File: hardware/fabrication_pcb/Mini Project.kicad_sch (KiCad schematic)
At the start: 14 parts, among them U1 DM-OLED096-636

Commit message: update footprints and symbols
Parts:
- ESP32, MIC1, Speaker1, amp1, nrf1: value ~ -> (none)

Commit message: feat: updated pcb layout
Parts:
- removed Speaker1: (no value), MyFootprints:0.25W_8OHM_SPEAKER, symbol MyComponents:SPEAKER
- added J1: Speaker, Connector_PinHeader_2.54mm:PinHeader_1x02_P2.54mm_Vertical, symbol Connector:Conn_01x02_Socket
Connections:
- net GND: now also C1.1, nrf1.1 (GND), J1.2 (Pin_2); no longer C1.2, nrf1.2 (VCC)
- net VCC: now also C1.2, nrf1.2 (VCC); no longer C1.1, nrf1.1 (GND)
- net at amp1.5 (OUT): now also J1.1 (Pin_1)
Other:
- title: (none) -> FELCOM-HW

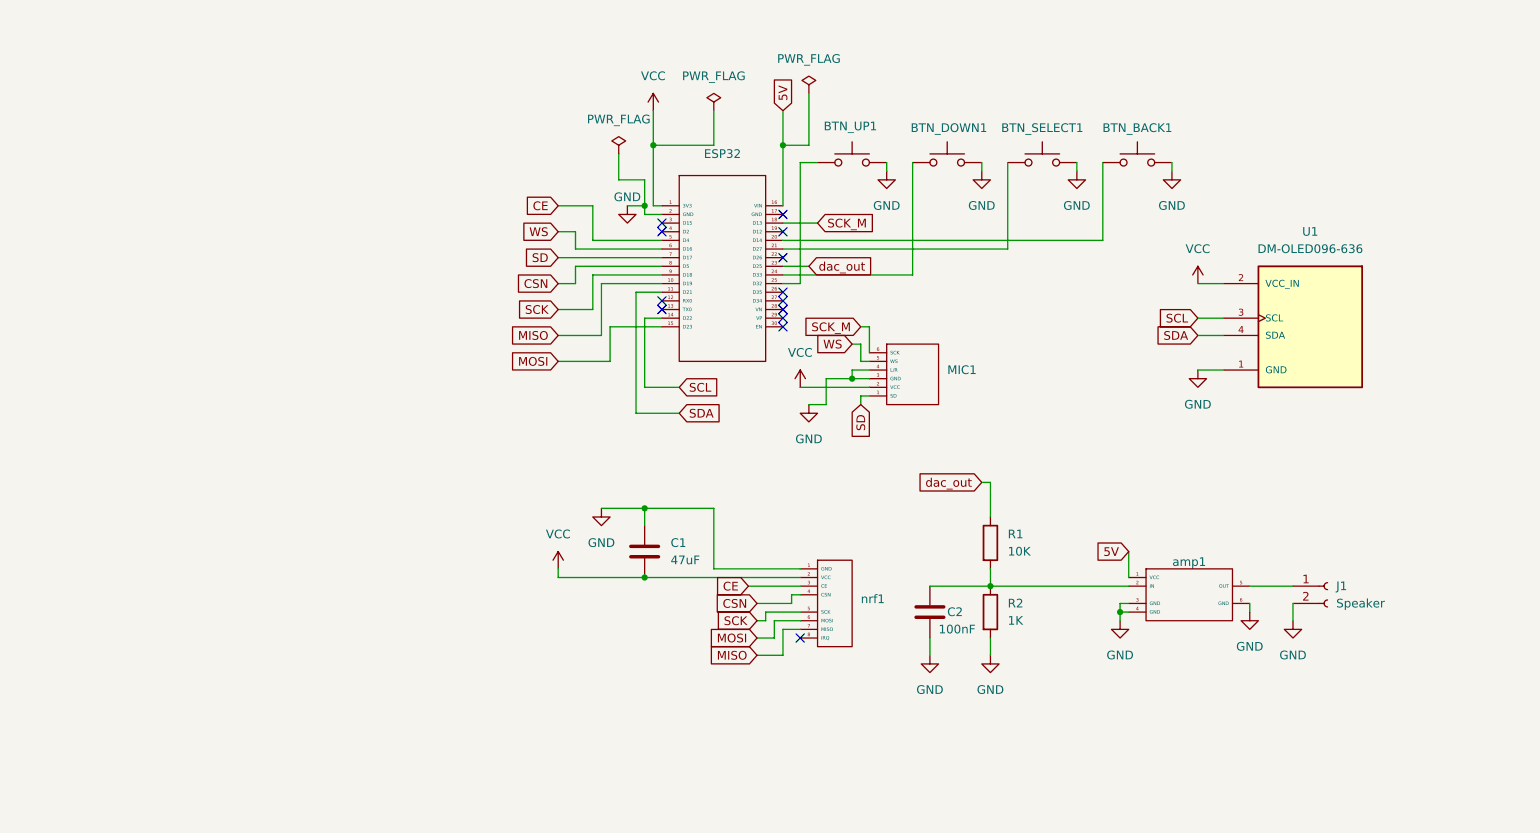
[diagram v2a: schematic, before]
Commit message: fix: schematic looking fancy, component placement done
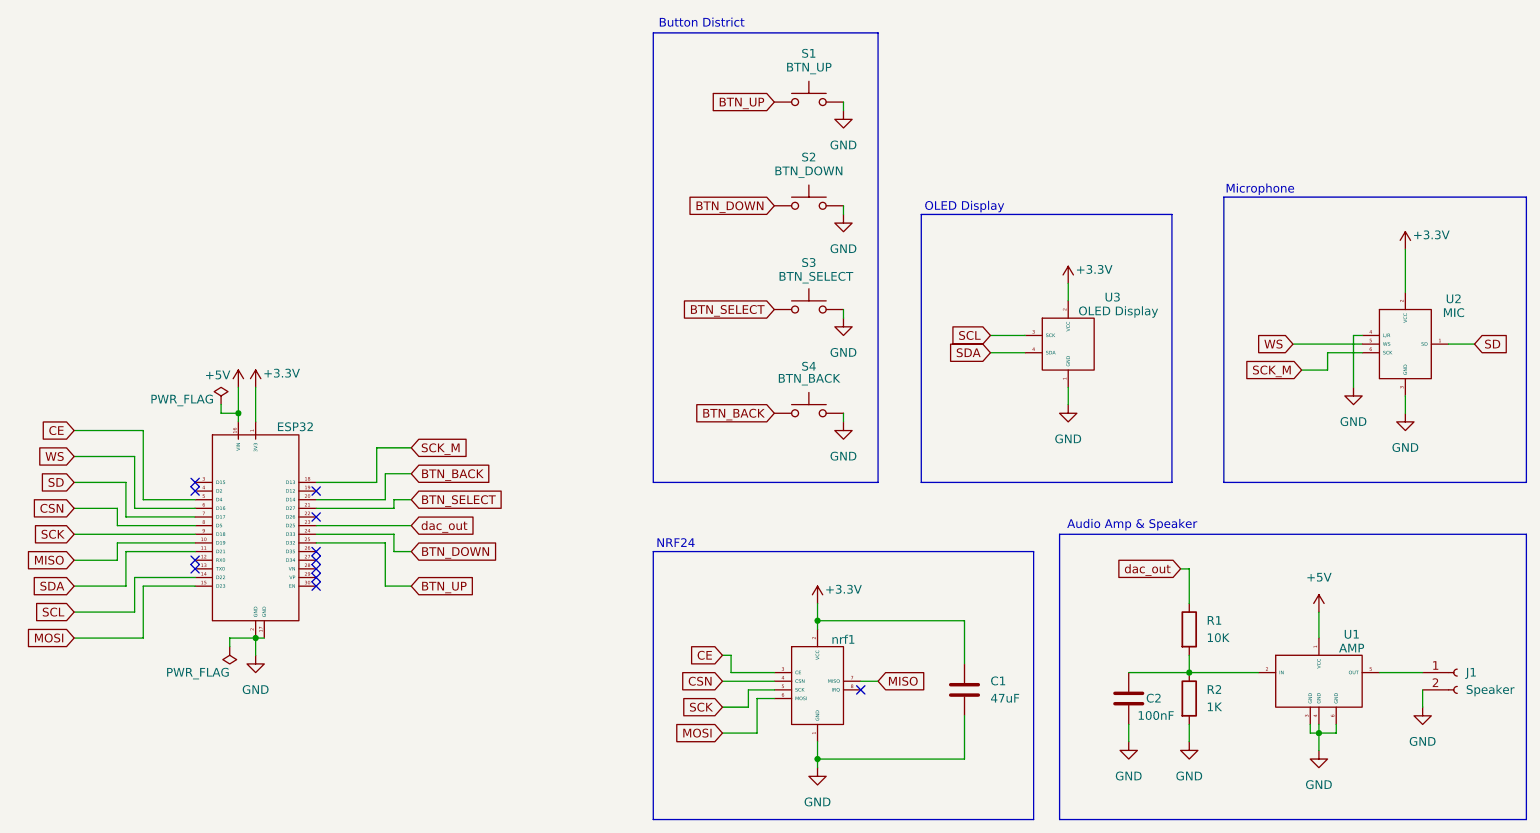
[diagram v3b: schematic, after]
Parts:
- removed MIC1: (no value), MyFootprints:MH-ET_I2S_MICROPHONE_MODULE, symbol MyComponents:MH-ET_I2S_MICROPHONE_MODULE
- removed U1: DM-OLED096-636, MyFootprints:MODULE_DM-OLED096-636, symbol DM-OLED096-636:DM-OLED096-636
- added U2: MIC, MyFootprints:MH-ET_I2S_MICROPHONE_MODULE, symbol MyComponents:MH-ET_I2S_MICROPHONE_MODULE
- added U3: OLED Display, MyFootprints:MODULE_DM-OLED096-636, symbol MyComponents:OLED_128x64_I2C
- S1: renamed from BTN_UP1; value SW_Push -> BTN_UP
- S2: renamed from BTN_DOWN1; value SW_Push -> BTN_DOWN
- S3: renamed from BTN_SELECT1; value SW_Push -> BTN_SELECT
- S4: renamed from BTN_BACK1; value SW_Push -> BTN_BACK
- U1: renamed from amp1; value (none) -> AMP
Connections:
- net GND: now also C1.2, ESP32.17 (GND), S2.1, U2.3 (GND), U2.4 (L/R), U3.1 (GND); no longer C1.1, S2.2
- net SCK_M: now also U2.6 (SCK)
- net SCL: now also U3.3 (SCK)
- net SD: now also U2.1 (SD)
- net SDA: now also U3.4 (SDA)
- net WS: now also U2.5 (WS)
- net BTN_DOWN: now reaches ESP32.24 (D33)
- net BTN_DOWN: now also S2.2; no longer S2.1
- net BTN_BACK: now reaches ESP32.20 (D14), S4.1
- net BTN_UP: now reaches ESP32.25 (D32), S1.1
- net BTN_SELECT: now reaches ESP32.21 (D27), S3.1
- net 5V renamed +5V
- net VCC renamed +3.3V
- net +3.3V: now also C1.1, U2.2 (VCC), U3.2 (VCC); no longer C1.2
- no-connect marks 13 -> 12
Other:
- note added: "Audio Amp & Speaker"
- note added: "Button District"
- note added: "Microphone"
- note added: "NRF24"
- note added: "OLED Display"
- moved on the sheet: C1, C2, ESP32, J1, R1, R2, S1, S2, S3, S4, U1, nrf1

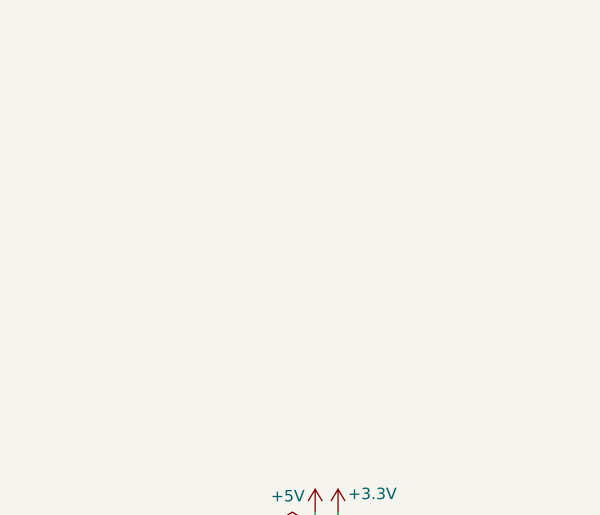
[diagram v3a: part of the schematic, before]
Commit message: feat: mount holes
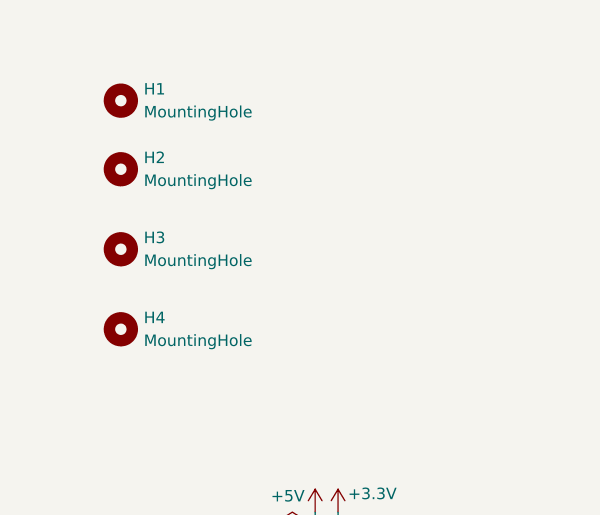
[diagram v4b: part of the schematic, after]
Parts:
- added H1, H2, H3, H4: MountingHole, MountingHole:MountingHole_3.2mm_M3, symbol Mechanical:MountingHole

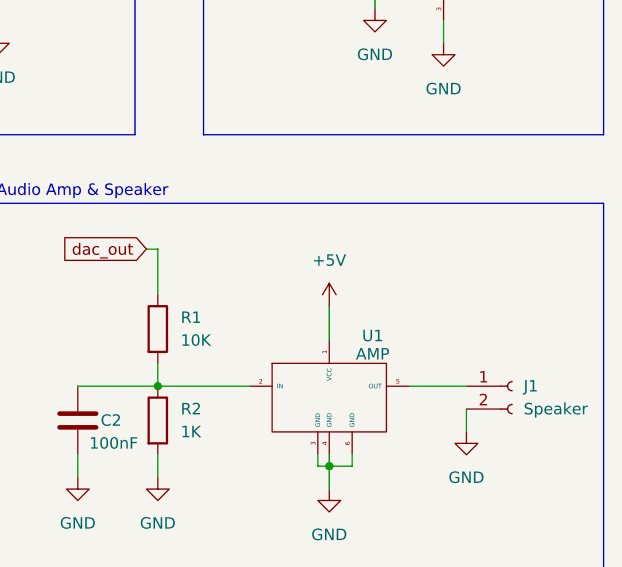
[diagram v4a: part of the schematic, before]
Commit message: Feat: silkscreen art
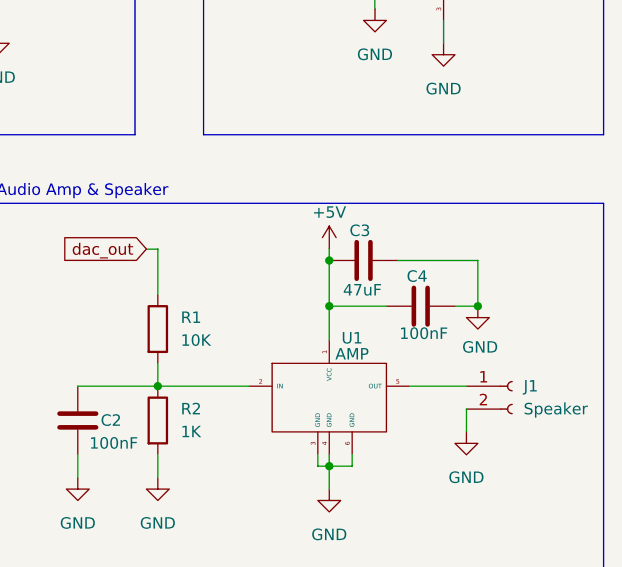
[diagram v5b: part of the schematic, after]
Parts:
- added C3: 47uF, Capacitor_THT:C_Disc_D5.0mm_W2.5mm_P2.50mm, symbol Device:C
- added C4: 100nF, Capacitor_THT:C_Disc_D5.0mm_W2.5mm_P2.50mm, symbol Device:C
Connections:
- net +5V: now also C3.1, C4.1
- net GND: now also C3.2, C4.2
